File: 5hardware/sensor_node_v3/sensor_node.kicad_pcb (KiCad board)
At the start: 2 copper layers, 37.5 x 100 mm, 18 parts, among them SW1 SW_DIP_x04, SW2 SW_DIP_x04, SW3 SW_Push, SW4 SW_Push, SW5 RotaryEncoder, U5 MCP1700x-330xxTO

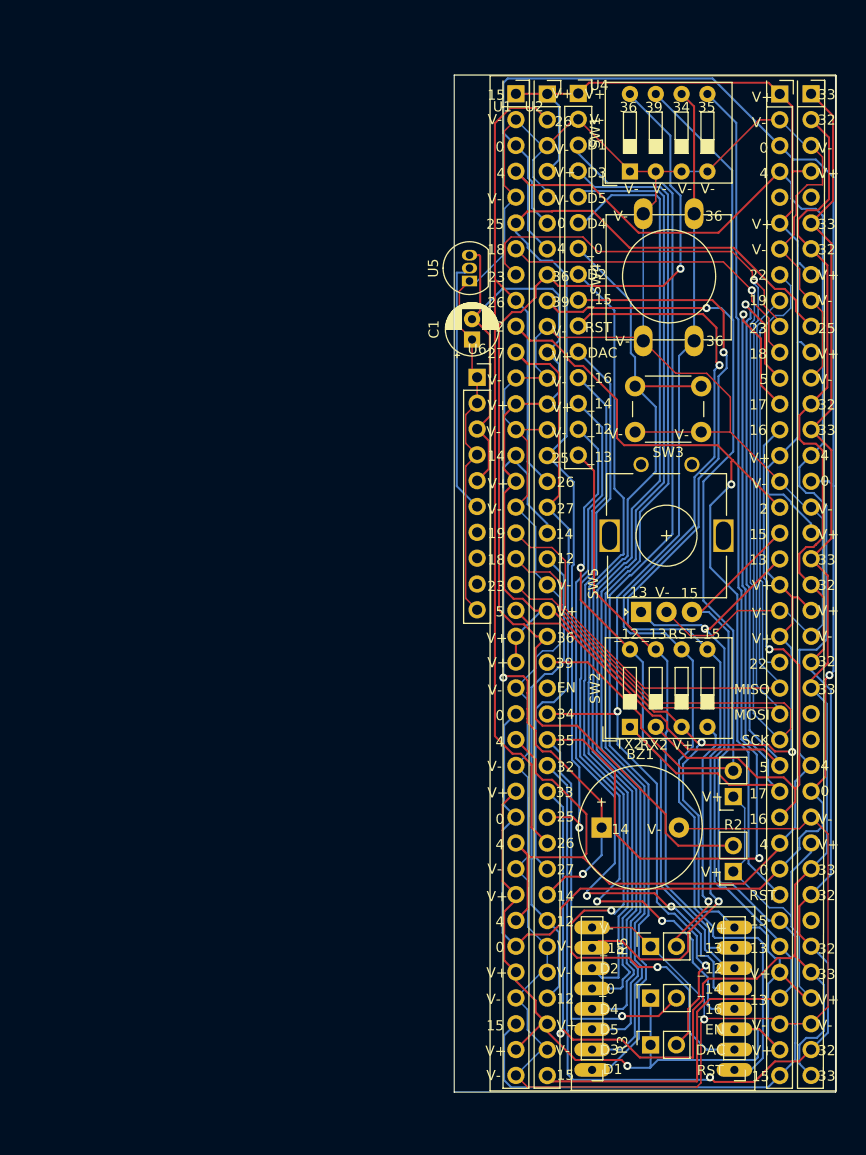
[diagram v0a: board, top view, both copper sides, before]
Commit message: added pcb design.
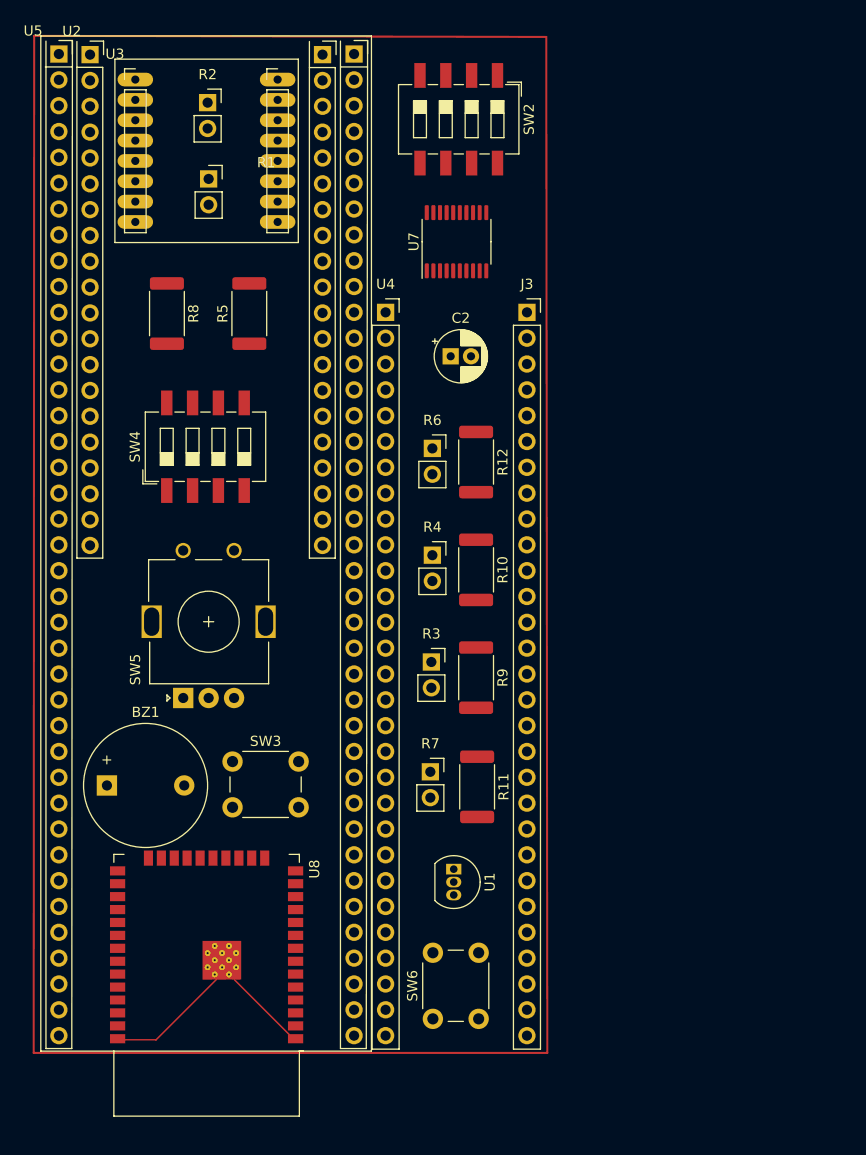
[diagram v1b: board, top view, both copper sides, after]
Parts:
- removed C1: C, Capacitor_THT:CP_Radial_D5.0mm_P2.00mm
- removed SW1: SW_DIP_x04, Button_Switch_THT:SW_DIP_SPSTx04_Slide_9.78x12.34mm_W7.62mm_P2.54mm
- removed U6: ~, Connector_PinSocket_2.54mm:PinSocket_1x10_P2.54mm_Vertical
- added C2: C, Capacitor_THT:CP_Radial_D5.0mm_P2.00mm, F.Cu at (126.9, 64.4)
- added J3: Conn_01x29, Connector_PinSocket_2.54mm:PinSocket_1x29_P2.54mm_Vertical, F.Cu at (134.4, 60.1)
- added R10: R, Resistor_SMD:R_2512_6332Metric, F.Cu at (129.4, 85.4)
- added R11: R, Resistor_SMD:R_2512_6332Metric, F.Cu at (129.5, 106.7)
- added R12: R, Resistor_SMD:R_2512_6332Metric, F.Cu at (129.4, 74.8)
- added R6: R, Connector_PinSocket_2.54mm:PinSocket_1x02_P2.54mm_Vertical, F.Cu at (125.1, 73.5)
- added R7: R, Connector_PinSocket_2.54mm:PinSocket_1x02_P2.54mm_Vertical, F.Cu at (124.9, 105.3)
- added R8: R, Resistor_SMD:R_2512_6332Metric, F.Cu at (99.0, 60.2)
- added R9: R, Resistor_SMD:R_2512_6332Metric, F.Cu at (129.4, 96.0)
- added SW6: SW_Push, Button_Switch_THT:SW_PUSH_6mm_H7.3mm, F.Cu at (125.2, 129.6)
- added U7: CH32V003F4P6, Package_SO:TSSOP-20_4.4x6.5mm_P0.65mm, F.Cu at (127.5, 53.1)
- added U8: ESP32-WROOM-32D, RF_Module:ESP32-WROOM-32D, F.Cu at (102.9, 123.3)
- R5: footprint Connector_PinSocket_2.54mm:PinSocket_1x02_P2.54mm_Vertical -> Resistor_SMD:R_2512_6332Metric
- SW2: footprint Button_Switch_THT:SW_DIP_SPSTx04_Slide_9.78x12.34mm_W7.62mm_P2.54mm -> Button_Switch_SMD:SW_DIP_SPSTx04_Slide_6.7x11.72mm_W8.61mm_P2.54mm_LowProfile
- SW4: value SW_Push -> SW_DIP_x04; footprint Button_Switch_THT:SW_PUSH-12mm -> Button_Switch_SMD:SW_DIP_SPSTx04_Slide_6.7x11.72mm_W8.61mm_P2.54mm_LowProfile
- U1: value ~ -> MCP1700x-330xxTO; footprint A_SensorNode:SensorBase -> Package_TO_SOT_THT:TO-92_Inline
- U4: footprint Connector_PinSocket_2.54mm:PinSocket_1x15_P2.54mm_Vertical -> Connector_PinSocket_2.54mm:PinSocket_1x29_P2.54mm_Vertical
- U5: value MCP1700x-330xxTO -> ~; footprint Package_TO_SOT_THT:TO-92_Inline -> A_SensorNode:SensorBase
- moved U3 119.3 mm to (93.9, 35.2), turned to 0 degrees
- moved R2 85.6 mm to (103.0, 39.5), turned to 0 degrees
- moved R1 85.4 mm to (103.1, 47.0), turned to 0 degrees
- moved U1 78.1 mm to (127.2, 114.8), turned to -90 degrees
- moved R5 73.7 mm to (107.1, 60.2)
- moved SW2 62.1 mm to (127.7, 41.1), turned to -90 degrees
- moved SW3 56.3 mm to (105.5, 104.2), turned to 0 degrees
- moved U5 49.2 mm to (85.8, 32.9), turned to 0 degrees
- moved BZ1 48.8 mm to (93.1, 106.6)
- moved R4 48.5 mm to (125.1, 84.0), turned to 0 degrees
- moved SW5 45.8 mm to (100.6, 98.0)
- moved U2 45.1 mm to (89.6, 32.9)
- moved SW4 44.3 mm to (102.8, 73.3)
- moved R3 43.4 mm to (125.0, 94.5), turned to 0 degrees
- moved U4 28.7 mm to (120.5, 60.1)
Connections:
- BZ1 pad 1: /OUT_0 -> OD0
- R1 pad 1: /VCC -> +3.3V
- R1 pad 2: Net-(R1-Pad2) -> IO_36
- R2 pad 1: /VCC -> +3.3V
- R2 pad 2: Net-(R2-Pad2) -> IO_k39
- R3 pad 1: /VCC -> +3.3V
- R3 pad 2: Net-(U2-IO_34) -> IO_34
- R4 pad 1: /VCC -> +3.3V
- R4 pad 2: Net-(U2-IO_35) -> IO_35
- R5 pad 1: GND -> +3.3V
- R5 pad 2: Net-(R5-Pad2) -> IO_36
- SW2 pad 1: /TX2 -> GND
- SW2 pad 2: /RX2 -> GND
- SW2 pad 3: /VCC -> GND
- SW2 pad 4: Net-(R5-Pad2) -> GND
- SW2 pad 5: Net-(U3-IO_15) -> Net-(U7-PD3)
- SW2 pad 6: Net-(U3-RST) -> Net-(U7-PD2)
- SW2 pad 7: Net-(U3-IO_13) -> Net-(U7-PD1)
- SW2 pad 8: Net-(U3-IO_12) -> Net-(U7-PD0)
- SW4 pad 1: GND -> BCLK
- SW4 pad 2: Net-(U2-IO_34) -> OD2 (26)
- SW5 pad A: /REF_1 -> Net-(J3-Pin_27)
- SW5 pad B: /REF_0 -> Net-(J3-Pin_29)
- U1 pad 1: /VCC -> GND
- U1 pad 2: GND -> +5V
- U1 pad 3: Net-(U2-IO_0) -> +3.3V
- U2 pad 1: /VCC -> GND
- U2 pad 10: GND -> SCL (32)
- U2 pad 11: /VCC -> SDA (33)
- U2 pad 12: GND -> OD1 (25)
- U2 pad 13: /VCC -> OD2 (26)
- U2 pad 14: GND -> BCLK
- U2 pad 15: /OUT_3 -> OD0 (14)
- U2 pad 16: /OUT_2 -> WLED (12)
- U2 pad 17: /OUT_1 -> GND
- U2 pad 18: /OUT_0 -> GND
- U2 pad 19: /WLED -> +3.3V
- U2 pad 2: /OUT_2 -> GND
- U2 pad 20: GND -> +3.3V
- U2 pad 21: /VCC -> GND
- U2 pad 22: Net-(R1-Pad2) -> GND
- U2 pad 23: Net-(R2-Pad2) -> +3.3V
- U2 pad 24: unconnected-(U2-EN-Pad24) -> +3.3V
- U2 pad 25: Net-(U2-IO_34) -> +3.3V
- U2 pad 26: Net-(U2-IO_35) -> LED (22)
- U2 pad 27: Net-(U2-IO_32) -> MISO (19)
- U2 pad 28: Net-(U2-IO_33) -> MOSI (23)
- U2 pad 29: /OUT_3 -> SCK (18)
- U2 pad 3: GND -> +3.3V
- U2 pad 30: /OUT_2 -> RST (5)
- U2 pad 31: /OUT_1 -> RX2 (17)
- U2 pad 32: /OUT_0 -> TX2 (16)
- U2 pad 33: /WLED -> LLED (4)
- U2 pad 34: GND -> SCL1 (0)
- U2 pad 35: GND -> SDA1 (2)
- U2 pad 36: /WLED -> OD5 (15)
- U2 pad 37: /VCC -> OD4 (13)
- U2 pad 38: GND -> +3.3V
- U2 pad 39: /REF_1 -> GND
- U2 pad 4: /VCC -> +3.3V
- U2 pad 40: /VCC -> GND
- U2 pad 5: GND -> IO_36
- U2 pad 6: Net-(U2-IO_0) -> IO_k39
- U2 pad 7: Net-(U2-IO_4) -> EN
- U2 pad 8: Net-(R1-Pad2) -> IO_34
- U2 pad 9: Net-(R2-Pad2) -> IO_35
- U3 pad 3: /VCC -> +3.3V
- U3 pad 8: /VCC -> +3.3V
- U4 pad 1: /VCC -> SDA (33)
- U4 pad 10: Net-(U3-RST) -> unconnected-(U4-x-Pad10)
- U4 pad 11: Net-(U3-ADC) -> +5V
- U4 pad 12: Net-(U3-IO_16) -> unconnected-(U4-x-Pad12)
- U4 pad 13: Net-(U3-IO_14) -> unconnected-(U4-x-Pad13)
- U4 pad 14: Net-(U3-IO_12) -> unconnected-(U4-x-Pad14)
- U4 pad 15: Net-(U3-IO_13) -> GND
- U4 pad 2: GND -> SCL (32)
- U4 pad 3: Net-(U3-D1_TX) -> GND
- U4 pad 4: Net-(U3-D3_RX) -> MISO (19)
- U4 pad 5: Net-(U3-D5_SCL) -> SCK (18)
- U4 pad 6: Net-(U3-D4_SDA) -> SDA (33)
- U4 pad 7: Net-(U3-IO_0) -> MOSI (23)
- U4 pad 8: Net-(U3-D2_LED) -> OD2
- U4 pad 9: Net-(U3-IO_15) -> +3.3V
- U5 pad 1: GND -> SDA1 (4)
- U5 pad 2: +5V -> SCL1 (0)
- U5 pad 3: /VCC -> GND
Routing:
- net GND: track 404.8 -> 21.2 mm, vias 1 -> 0
- net /VCC: track 377.9 -> 0.00 mm, vias 3 -> 0
- net Net-(U2-IO_0): track 181.5 -> 0.00 mm, vias 1 -> 0
- net Net-(U2-IO_4): track 168.0 -> 0.00 mm
- net Net-(U2-IO_33): track 164.8 -> 0.00 mm, vias 1 -> 0
- net Net-(U2-IO_32): track 161.8 -> 0.00 mm, vias 1 -> 0
- net Net-(U2-IO_35): track 146.1 -> 0.00 mm, vias 2 -> 0
- net /SCK: track 116.4 -> 0.00 mm, vias 1 -> 0
- net Net-(R2-Pad2): track 114.8 -> 0.00 mm, vias 1 -> 0
- net /MOSI: track 111.8 -> 0.00 mm, vias 1 -> 0
- net Net-(U2-IO_34): track 109.4 -> 0.00 mm, vias 2 -> 0
- net Net-(R1-Pad2): track 109.0 -> 0.00 mm, vias 1 -> 0
- net Net-(U3-D1_TX): track 105.9 -> 0.00 mm
- net Net-(U3-RST): track 105.0 -> 0.00 mm, vias 1 -> 0
- net /OUT_3: track 103.1 -> 0.00 mm, vias 1 -> 0
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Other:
- board outline removed
- board text removed: "16"
- board text removed: "17"
- board text removed: "18"
- board text removed: "19"
- board text removed: "2"
- board text removed: "23"

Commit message: updating pcb design.
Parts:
- added J1: Conn_01x03, Connector_PinHeader_2.54mm:PinHeader_1x03_P2.54mm_Vertical, F.Cu at (96.2, 88.0)
- BZ1: footprint Buzzer_Beeper:Buzzer_12x9.5RM7.6 -> A_SensorNode:BuzzerSmall
- SW6: footprint Button_Switch_THT:SW_PUSH_6mm_H7.3mm -> Button_Switch_THT:SW_PUSH-12mm
- moved SW3 31.7 mm to (125.3, 128.9), turned to 90 degrees
- moved SW6 25.1 mm to (113.3, 107.4), turned to 180 degrees
- moved SW5 14.1 mm to (113.9, 93.3), turned to 180 degrees
- moved BZ1 2.34 mm to (94.6, 104.8)
- moved U7 0.87 mm to (127.9, 53.9)
- moved SW4 0.38 mm to (103.0, 73.6), turned to -90 degrees
- moved R5 0.33 mm to (107.3, 59.9)
- moved R8 0.33 mm to (99.2, 59.9)
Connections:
- J3 pad 10: unconnected-(J3-Pin_10-Pad10) -> Net-(J1-Pin_2)
- J3 pad 11: unconnected-(J3-Pin_11-Pad11) -> Net-(J1-Pin_3)
- J3 pad 9: unconnected-(J3-Pin_9-Pad9) -> Net-(J1-Pin_1)
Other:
- board text removed: "5V"

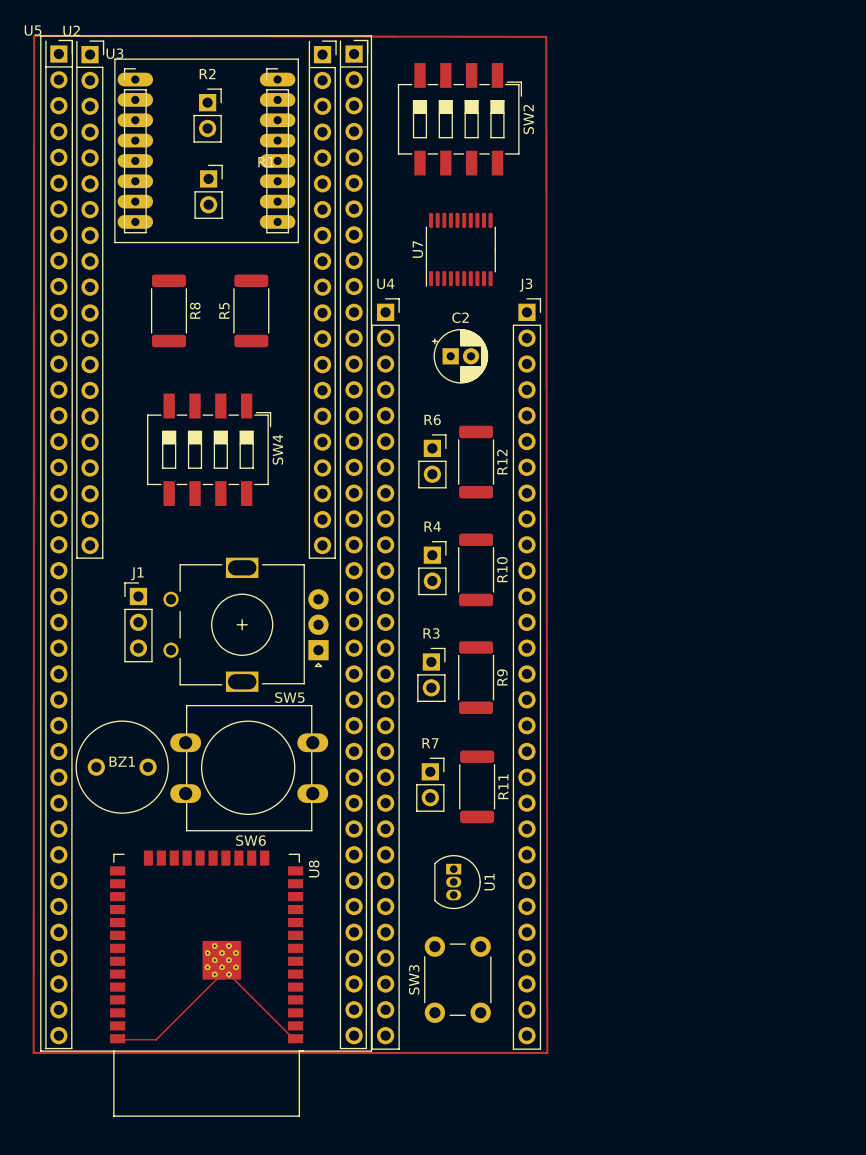
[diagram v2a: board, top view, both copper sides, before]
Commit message: updated schematic. ESP32-C3 support.
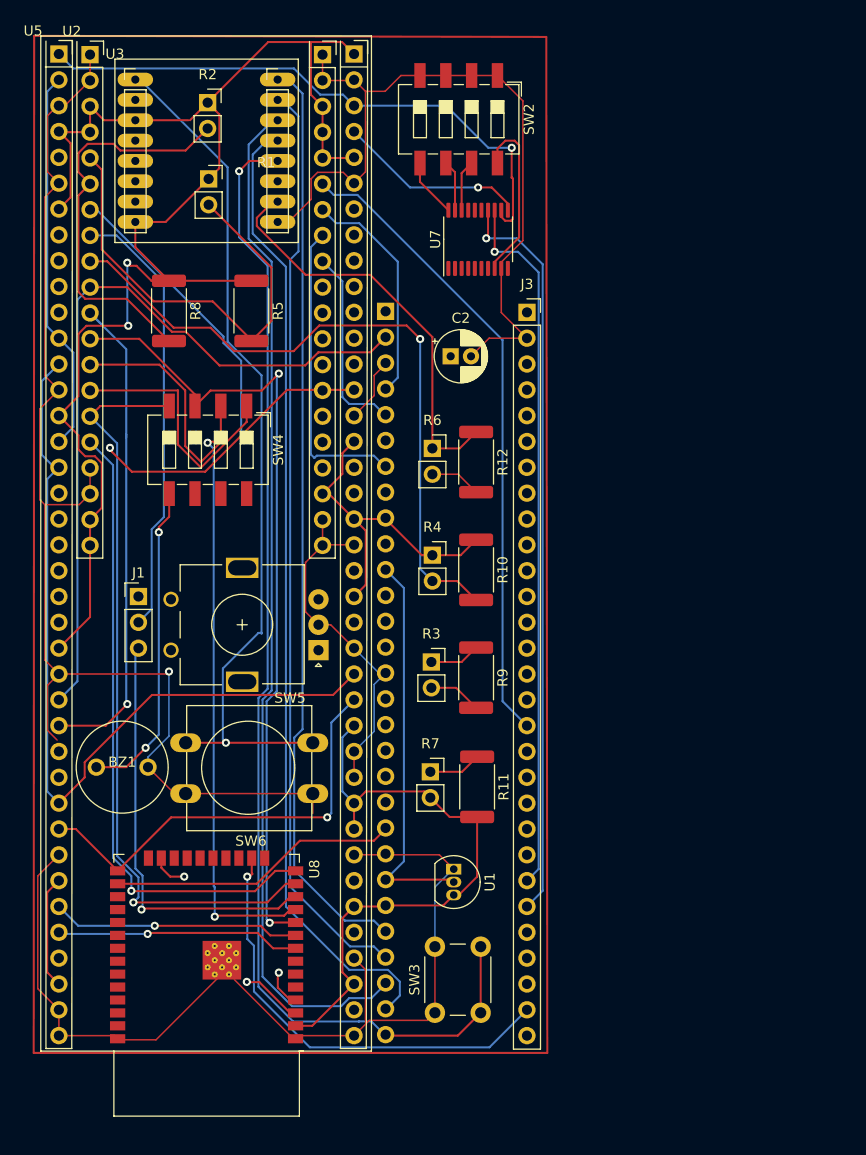
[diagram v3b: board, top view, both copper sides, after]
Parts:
- U4: moved to B.Cu
- moved U7 1.97 mm to (129.6, 52.9)
- moved U4 0.10 mm to (120.5, 60.0), turned to 180 degrees
- turned R5 to -90 degrees
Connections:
- J1 pad 1: Net-(J1-Pin_1) -> unconnected-(J1-Pin_1-Pad1)
- J1 pad 2: Net-(J1-Pin_2) -> IO_34
- J1 pad 3: Net-(J1-Pin_3) -> BCLK
- J3 pad 10: Net-(J1-Pin_2) -> unconnected-(J3-Pin_10-Pad10)
- J3 pad 11: Net-(J1-Pin_3) -> unconnected-(J3-Pin_11-Pad11)
- J3 pad 9: Net-(J1-Pin_1) -> unconnected-(J3-Pin_9-Pad9)
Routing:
- net GND: track 21.2 -> 338.7 mm, vias 0 -> 1
- net +3.3V: track 0.00 -> 253.2 mm, vias 0 -> 2
- net SDA1 (4): track 0.00 -> 139.3 mm, vias 0 -> 1
- net SCL1 (0): track 0.00 -> 127.8 mm, vias 0 -> 3
- net Net-(U3-IO_0): track 0.00 -> 117.2 mm, vias 0 -> 1
- net Net-(U3-D5_SCL): track 0.00 -> 101.2 mm
- net SCL (32): track 0.00 -> 99.3 mm, vias 0 -> 1
- net Net-(U3-D4_SDA): track 0.00 -> 95.9 mm
- net Net-(U3-D3_RX): track 0.00 -> 91.6 mm
- net Net-(U3-D1_TX): track 0.00 -> 91.2 mm
- net Net-(U3-RST): track 0.00 -> 90.3 mm, vias 0 -> 1
- net OD2 (26): track 0.00 -> 80.8 mm, vias 0 -> 2
- net OD1 (25): track 0.00 -> 80.5 mm, vias 0 -> 2
- net OD0 (14): track 0.00 -> 74.9 mm, vias 0 -> 1
- net SDA (33): track 0.00 -> 74.0 mm, vias 0 -> 2
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
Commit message: updating pcb design.
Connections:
- C2 pad 1: +3.3V -> EN
- J3 pad 1: +3.3V -> EN
- J3 pad 10: unconnected-(J3-Pin_10-Pad10) -> RX (3)
- J3 pad 11: unconnected-(J3-Pin_11-Pad11) -> TX (1)
- J3 pad 19: FREE (21) -> AUD (21)
- J3 pad 3: unconnected-(J3-Pin_3-Pad3) -> OD1
- J3 pad 5: unconnected-(J3-Pin_5-Pad5) -> OD0
- J3 pad 9: unconnected-(J3-Pin_9-Pad9) -> OD2
- R1 pad 1: +3.3V -> EN
- R10 pad 1: +3.3V -> EN
- R11 pad 2: +3.3V -> EN
- R2 pad 1: +3.3V -> EN
- R2 pad 2: IO_k39 -> IO_39
- R3 pad 1: +3.3V -> EN
- R4 pad 1: +3.3V -> EN
- R5 pad 1: +3.3V -> EN
- R7 pad 2: +3.3V -> EN
- R8 pad 1: +3.3V -> EN
- R8 pad 2: IO_k39 -> IO_39
- R9 pad 1: +3.3V -> EN
- SW4 pad 1: BCLK -> OD3 (27)
- SW4 pad 8: OD3 -> BCLK
- U1 pad 3: +3.3V -> EN
- U2 pad 14: BCLK -> OD3 (27)
- U2 pad 19: +3.3V -> EN
- U2 pad 20: +3.3V -> EN
- U2 pad 23: +3.3V -> EN
- U2 pad 24: +3.3V -> EN
- U2 pad 25: +3.3V -> EN
- U2 pad 3: +3.3V -> EN
- U2 pad 38: +3.3V -> EN
- U2 pad 4: +3.3V -> EN
- U2 pad 6: IO_k39 -> IO_39
- U3 pad 3: +3.3V -> EN
- U3 pad 8: +3.3V -> EN
- U4 pad 24: +3.3V -> EN
- U4 pad 3: GND -> EN
- U4 pad 4: MISO (19) -> GND
- U4 pad 5: SCK (18) -> MISO (19)
- U4 pad 6: SDA (33) -> SCK (18)
- U4 pad 9: +3.3V -> EN
- U5 pad 1: SDA1 (4) -> SDA1 (2)
- U5 pad 10: unconnected-(U5-A+-Pad10) -> AUD (21)
- U5 pad 13: SDA1 (4) -> SDA1 (2)
- U5 pad 15: +3.3V -> EN
- U5 pad 17: SDA1 (4) -> SDA1 (2)
- U5 pad 18: unconnected-(U5-_RES-Pad18) -> GND
- U5 pad 19: unconnected-(U5-_DC-Pad19) -> EN
- U5 pad 21: unconnected-(U5-_LED-Pad21) -> SDA1 (2)
- U5 pad 22: unconnected-(U5-x-Pad22) -> SCL1 (0)
- U5 pad 23: unconnected-(U5-x-Pad23) -> GND
- U5 pad 24: +3.3V -> EN
- U5 pad 30: SDA1 (4) -> SDA1 (2)
- U5 pad 33: +3.3V -> EN
- U5 pad 36: unconnected-(U5-PIR-Pad36) -> IO_39
- U5 pad 37: +3.3V -> EN
- U5 pad 4: +3.3V -> EN
- U5 pad 40: +3.3V -> EN
- U5 pad 42: SDA1 (4) -> SDA1 (2)
- U5 pad 44: +3.3V -> EN
- U5 pad 48: unconnected-(U5-DIN-Pad48) -> IO_34
- U5 pad 5: AUD -> unconnected-(U5-_OUT-Pad5)
- U5 pad 51: unconnected-(U5-x-Pad51) -> TX2 (16)
- U5 pad 52: SDA1 (4) -> SDA1 (2)
- U5 pad 55: +3.3V -> EN
- U5 pad 56: unconnected-(U5-x-Pad56) -> RX2 (17)
- U5 pad 58: +3.3V -> EN
- U5 pad 61: +3.3V -> EN
- U5 pad 62: unconnected-(U5-WS28-Pad62) -> WLED (12)
- U5 pad 64: SDA1 (4) -> SDA1 (2)
- U5 pad 66: +3.3V -> EN
- U5 pad 69: +3.3V -> EN
- U5 pad 7: +3.3V -> EN
- U5 pad 70: +3.3V -> EN
- U5 pad 71: GND -> WLED (12)
- U5 pad 72: unconnected-(U5-OUT-Pad72) -> GND
- U5 pad 73: +3.3V -> EN
- U5 pad 74: unconnected-(U5-OUT-Pad74) -> IO_35
- U5 pad 76: +3.3V -> EN
- U5 pad 77: unconnected-(U5-OUT-Pad77) -> GND
- U5 pad 78: GND -> IO_36
- U5 pad 9: unconnected-(U5-A--Pad9) -> GND
- U7 pad 12: SDA1 (4) -> SDA1 (2)
- U7 pad 4: OD3 -> BCLK
- U7 pad 7: +3.3V -> EN
- U8 pad 12: BCLK -> OD3 (27)
- U8 pad 2: +3.3V -> EN
- U8 pad 33: FREE (21) -> AUD (21)
- U8 pad 34: RX -> RX (3)
- U8 pad 35: TX -> TX (1)
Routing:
- net EN: track 35.6 -> 317.3 mm, vias 1 -> 4
- net +3.3V: track 253.2 -> 0.00 mm, vias 2 -> 0
- net SDA1 (2): track 0.00 -> 164.5 mm, vias 0 -> 3
- net SDA1 (4): track 139.3 -> 0.00 mm, vias 1 -> 0
- net IO_39: track 0.00 -> 123.2 mm, vias 0 -> 3
- net RX (3): track 0.00 -> 84.0 mm, vias 0 -> 2
- net Net-(J3-Pin_25): track 0.00 -> 80.8 mm, vias 0 -> 2
- net TX (1): track 0.00 -> 78.9 mm, vias 0 -> 3
- net LED (22): track 63.0 -> 139.4 mm, vias 0 -> 1
- net IO_34: track 48.8 -> 123.6 mm, vias 0 -> 2
- net IO_36: track 48.5 -> 119.7 mm, vias 1 -> 3
- net AUD (21): track 0.00 -> 64.4 mm, vias 0 -> 4
- net Net-(J3-Pin_21): track 0.00 -> 63.1 mm, vias 0 -> 1
- net Net-(J3-Pin_22): track 0.00 -> 61.1 mm, vias 0 -> 1
- net Net-(J3-Pin_29): track 0.00 -> 61.0 mm, vias 0 -> 2
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
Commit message: update pcb wirings.
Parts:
- moved U7 2.61 mm to (127.0, 52.7)
- moved J3 1.30 mm to (133.1, 60.1)
- moved C2 0.86 mm to (126.0, 64.3)
- moved SW3 0.80 mm to (124.5, 128.9)
- moved U1 0.80 mm to (126.4, 114.8)
- moved SW2 0.78 mm to (127.1, 40.6)
- moved R11 0.70 mm to (128.8, 106.7)
- moved R9 0.60 mm to (128.8, 95.9)
- moved R10 0.60 mm to (128.8, 85.4)
- moved R12 0.50 mm to (128.9, 74.8)
- moved R4 0.20 mm to (124.9, 84.0)
- moved R6 0.20 mm to (124.9, 73.5)
- moved U4 0.10 mm to (120.5, 60.1)
- moved R3 0.10 mm to (124.9, 94.5)
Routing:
- net RX2 (17): track 0.00 -> 85.3 mm, vias 0 -> 2
- net OD1: track 11.7 -> 73.1 mm, vias 1 -> 5
- net OD3 (27): track 25.1 -> 84.4 mm, vias 0 -> 2
- net SCL1 (0): track 128.0 -> 185.2 mm, vias 3 -> 5
- net SDA1 (2): track 164.5 -> 220.5 mm, vias 3 -> 5
- net OD4 (13): track 45.3 -> 98.9 mm, vias 2 -> 4
- net RX (3): track 84.0 -> 35.7 mm
- net LLED (4): track 28.6 -> 73.1 mm, vias 0 -> 2
- net IO_34: track 123.6 -> 159.1 mm, vias 2 -> 3
- net Net-(U3-IO_15): track 20.4 -> 46.2 mm, vias 0 -> 2
- net RST (5): track 41.6 -> 66.0 mm
- net OD0: track 61.6 -> 83.9 mm, vias 1 -> 3
- net SCK (18): track 71.4 -> 89.0 mm
- net TX2 (16): track 0.00 -> 16.6 mm, vias 0 -> 1
- net BCLK: track 78.4 -> 92.9 mm
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
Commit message: update pcb design.
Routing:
- net GND: track 351.5 -> 424.6 mm, vias 6 -> 8
- net MISO (19): track 36.0 -> 108.0 mm, vias 0 -> 2
- net IO_39: track 123.0 -> 190.1 mm, vias 3 -> 4
- net EN: track 323.2 -> 390.0 mm
- net TX2 (16): track 16.6 -> 81.5 mm, vias 1 -> 2
- net AUD (21): track 63.0 -> 126.9 mm
- net RST (5): track 66.0 -> 123.9 mm
- net IO_35: track 80.3 -> 138.1 mm, vias 2 -> 5
- net OD5 (15): track 43.3 -> 93.3 mm, vias 2 -> 4
- net MOSI (23): track 89.0 -> 137.8 mm, vias 2 -> 6
- net OD0: track 83.9 -> 132.5 mm, vias 3 -> 4
- net RX (3): track 35.7 -> 83.1 mm, vias 2 -> 4
- net SDA (33): track 91.5 -> 138.9 mm, vias 3 -> 5
- net Net-(J3-Pin_27): track 53.7 -> 99.3 mm, vias 2 -> 3
- net Net-(J3-Pin_29): track 61.3 -> 104.9 mm, vias 2 -> 3
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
